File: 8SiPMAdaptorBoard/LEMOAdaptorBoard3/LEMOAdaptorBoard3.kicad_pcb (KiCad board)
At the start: 2 copper layers, 58.8 x 63 mm, 32 parts

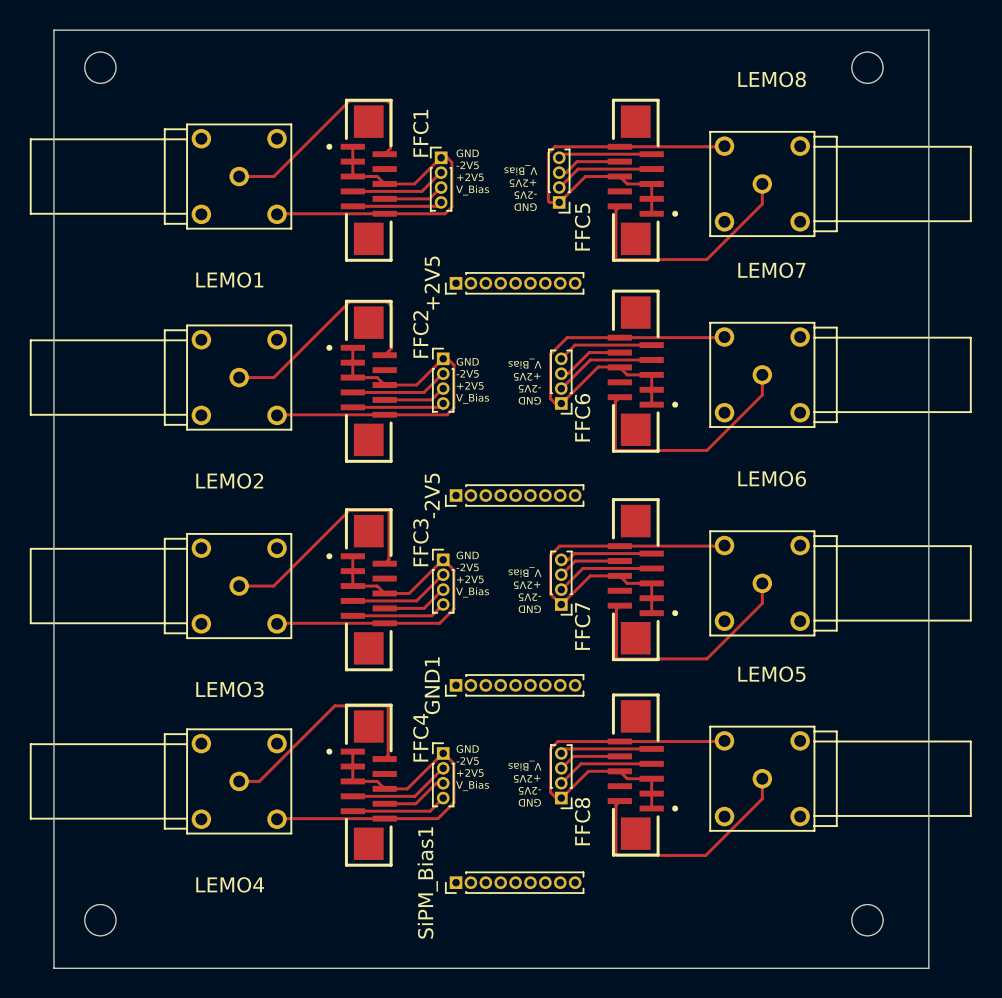
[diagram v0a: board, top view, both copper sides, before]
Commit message: More LEMO adaptor design
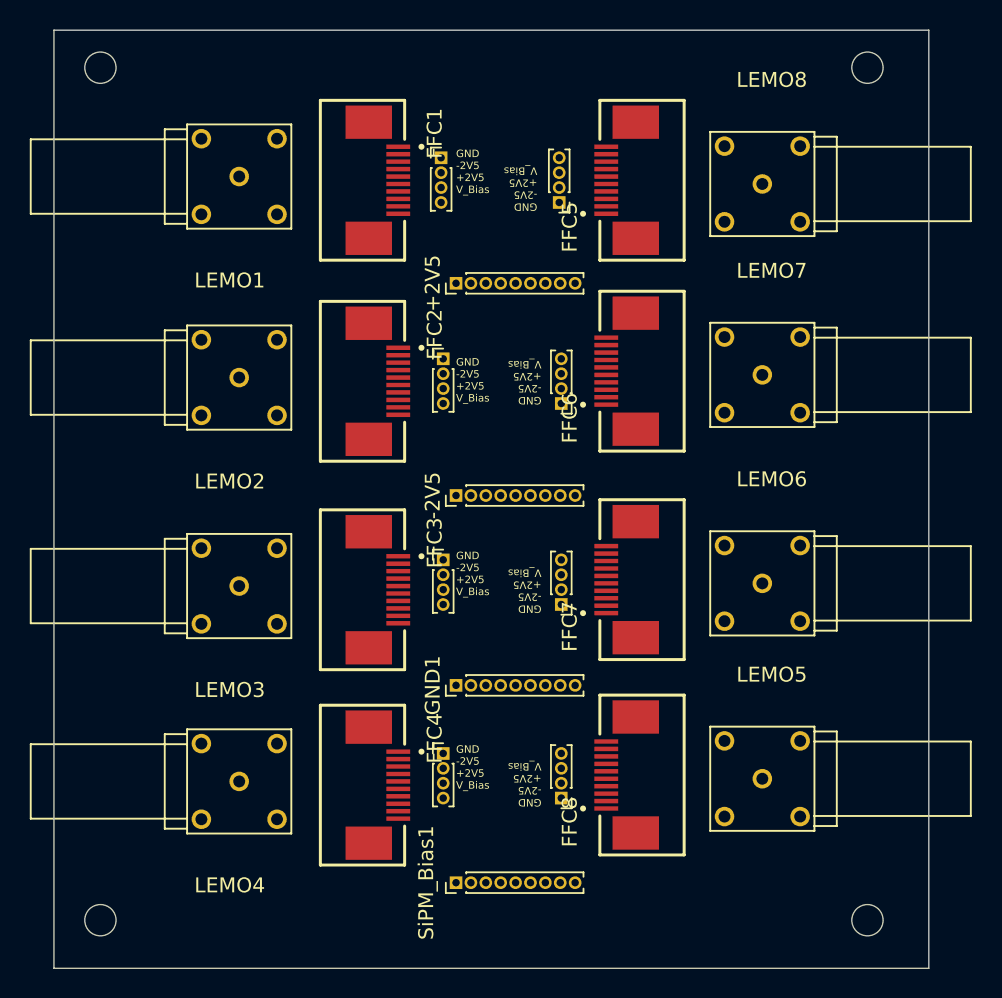
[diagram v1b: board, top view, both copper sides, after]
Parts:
- FFC1, FFC2, FFC3, FFC4, FFC5, FFC6, FFC7, FFC8: footprint FFC_10position_vertical:SAMTEC_ZF5S-10-03-T-WT -> FFC_10position_connector:SAMTEC_ZF5S-10-01-T-WT
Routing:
- net Net-(PIN7-Pin_1): track 25.3 -> 0.00 mm
- net Net-(PIN4-Pin_1): track 25.2 -> 0.00 mm
- net Net-(PIN8-Pin_1): track 25.1 -> 0.00 mm
- net Net-(PIN3-Pin_1): track 25.1 -> 0.00 mm
- net Net-(PIN2-Pin_1): track 24.9 -> 0.00 mm
- net Net-(PIN5-Pin_1): track 24.7 -> 0.00 mm
- net Net-(PIN1-Pin_1): track 24.7 -> 0.00 mm
- net Net-(PIN6-Pin_1): track 24.6 -> 0.00 mm
- net Net-(FFC8-Signal-Pad02): track 16.4 -> 0.00 mm
- net Net-(FFC6-Signal-Pad02): track 16.4 -> 0.00 mm
- net Net-(FFC5-Signal-Pad02): track 16.4 -> 0.00 mm
- net Net-(FFC7-Signal-Pad02): track 16.4 -> 0.00 mm
- net Net-(FFC2-Signal-Pad02): track 15.9 -> 0.00 mm
- net Net-(FFC1-Signal-Pad02): track 15.9 -> 0.00 mm
- net Net-(FFC3-Signal-Pad02): track 15.8 -> 0.00 mm
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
